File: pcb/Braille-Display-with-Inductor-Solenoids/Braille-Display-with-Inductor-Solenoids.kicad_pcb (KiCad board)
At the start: 2 copper layers, 58.2 x 57.4 mm, 60 parts, among them J1 Screw_Terminal_01x02, J2 Screw_Terminal_01x02, J3 Screw_Terminal_01x02, SW1 SW_Push, SW2 SW_Push, U1 RP2040-Zero, U2 TPIC6595, U3 TPIC6595, U4 TPIC6595

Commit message: Remove symbol and footprint libraries
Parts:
- L1, L10, L11, L12, L13, L14, L15, L16, L17, L18, L2, L3, L4, L5, L6, L7, L8, L9: footprint 00-project-footprint-lib:Inductor_0805_2012Metric_SMD_Vertical_Square -> 00-project-footprints:Inductor_0805_2012Metric_SMD_Vertical_Square
- SW1, SW2: footprint 00-project-footprint-lib:PushButtonSMD_2.93x3.9 -> 00-project-footprints:PushButtonSMD_2.93x3.9
- U1: footprint 00-project-footprint-lib:RP2040 Zero -> 00-project-footprints:RP2040 Zero

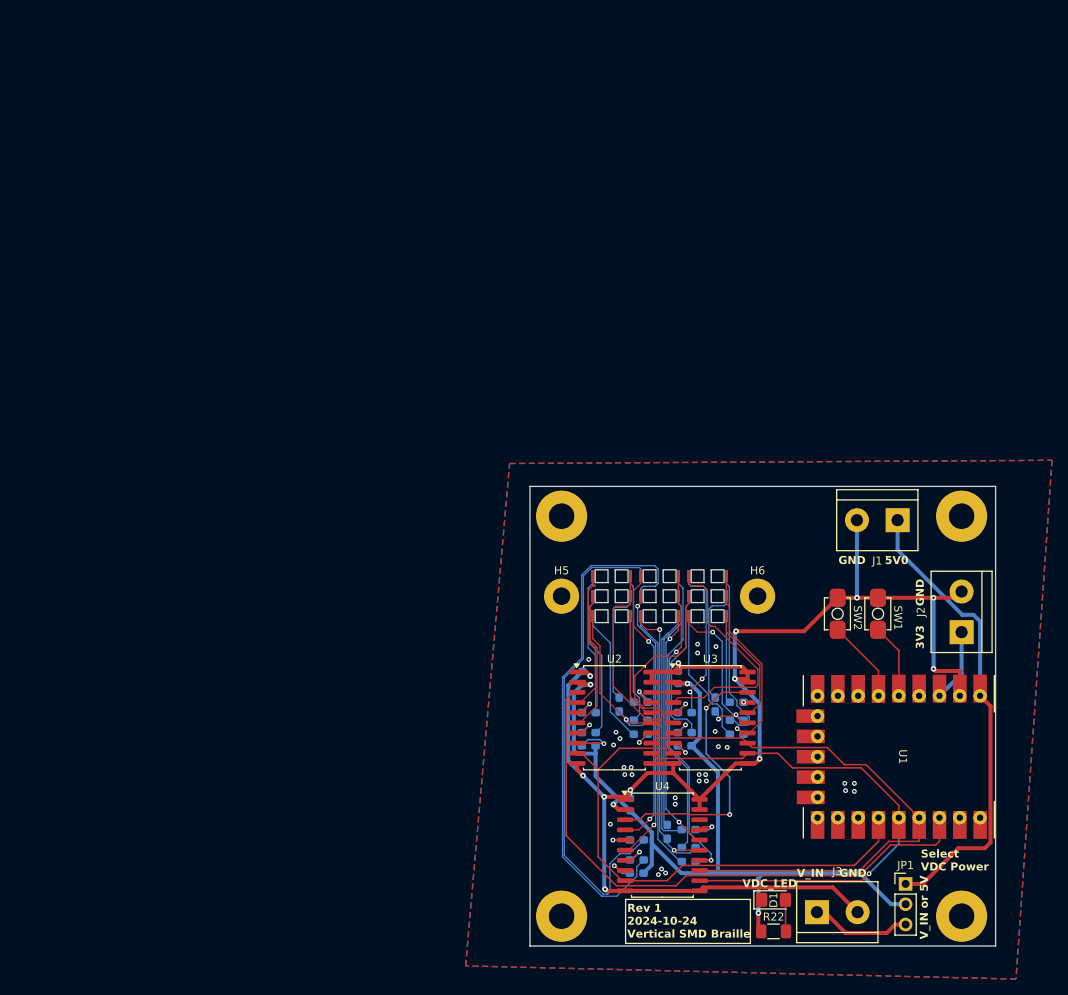
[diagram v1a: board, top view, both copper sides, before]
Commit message: Add both inductors on same PCB, switch to new drivers
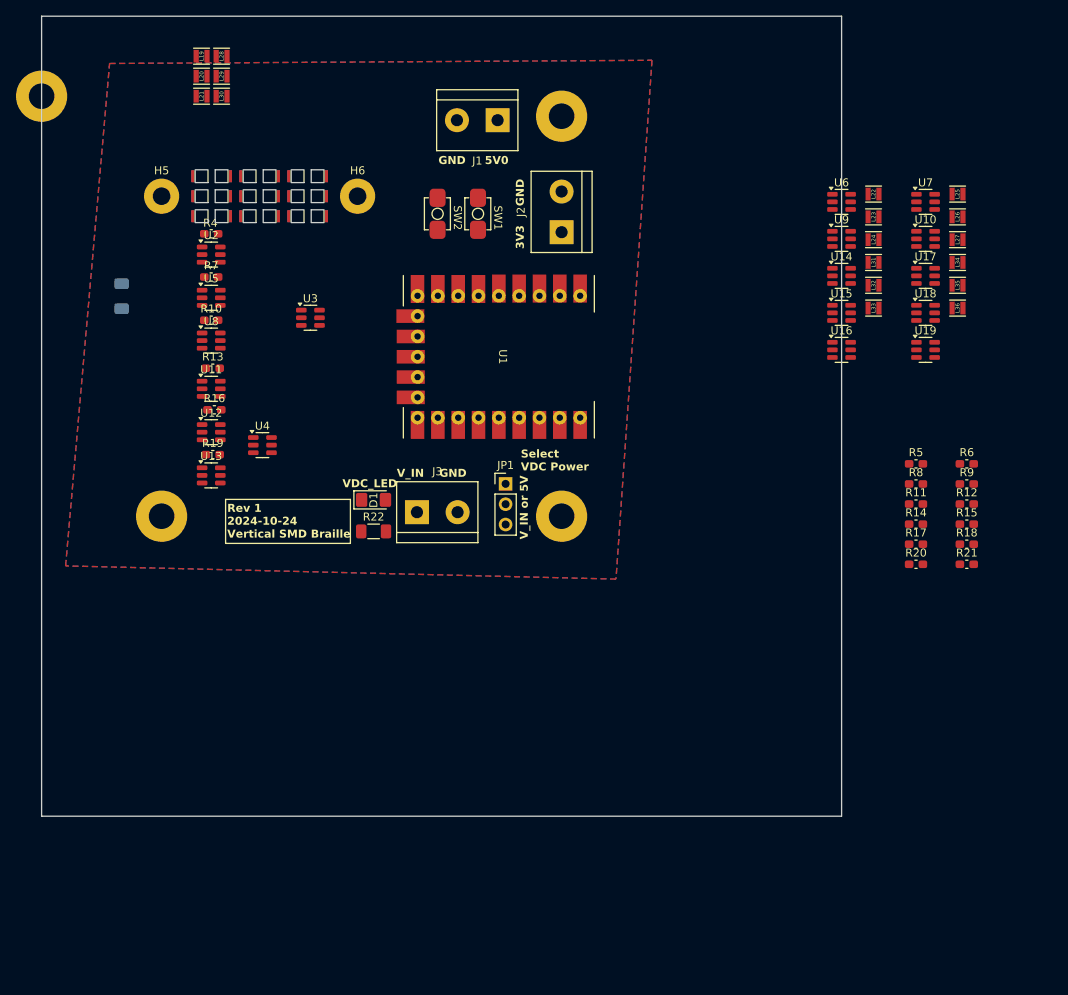
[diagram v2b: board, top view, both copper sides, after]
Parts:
- removed C2, C3: 100n, Capacitor_SMD:C_0603_1608Metric
- removed R1, R2, R3: 10k, Capacitor_SMD:C_0603_1608Metric_Pad1.08x0.95mm_HandSolder
- added L19: L, 00-project-footprints:Inductor_VLS201612CX, F.Cu at (50.0, 35.0)
- added L20: L, 00-project-footprints:Inductor_VLS201612CX, F.Cu at (50.0, 37.5)
- added L21: L, 00-project-footprints:Inductor_VLS201612CX, F.Cu at (50.0, 40.0)
- added L22: L, 00-project-footprints:Inductor_VLS201612CX, F.Cu at (134.0, 52.2)
- added L23: L, 00-project-footprints:Inductor_VLS201612CX, F.Cu at (134.0, 55.1)
- added L24: L, 00-project-footprints:Inductor_VLS201612CX, F.Cu at (134.0, 57.9)
- added L25: L, 00-project-footprints:Inductor_VLS201612CX, F.Cu at (144.5, 52.2)
- added L26: L, 00-project-footprints:Inductor_VLS201612CX, F.Cu at (144.5, 55.1)
- added L27: L, 00-project-footprints:Inductor_VLS201612CX, F.Cu at (144.5, 57.9)
- added L28: L, 00-project-footprints:Inductor_VLS201612CX, F.Cu at (52.5, 35.0)
- added L29: L, 00-project-footprints:Inductor_VLS201612CX, F.Cu at (52.5, 37.5)
- added L30: L, 00-project-footprints:Inductor_VLS201612CX, F.Cu at (52.5, 40.0)
- added L31: L, 00-project-footprints:Inductor_VLS201612CX, F.Cu at (134.0, 60.8)
- added L32: L, 00-project-footprints:Inductor_VLS201612CX, F.Cu at (134.0, 63.6)
- added L33: L, 00-project-footprints:Inductor_VLS201612CX, F.Cu at (134.0, 66.5)
- added L34: L, 00-project-footprints:Inductor_VLS201612CX, F.Cu at (144.5, 60.8)
- added L35: L, 00-project-footprints:Inductor_VLS201612CX, F.Cu at (144.5, 63.6)
- added L36: L, 00-project-footprints:Inductor_VLS201612CX, F.Cu at (144.5, 66.5)
- added U10: AD116, Package_TO_SOT_SMD:SOT-23-6, F.Cu at (140.5, 57.8)
- added U11: AD116, Package_TO_SOT_SMD:SOT-23-6, F.Cu at (51.2, 76.6)
- added U12: AD116, Package_TO_SOT_SMD:SOT-23-6, F.Cu at (51.2, 82.0)
- added U13: AD116, Package_TO_SOT_SMD:SOT-23-6, F.Cu at (51.2, 87.4)
- added U14: AD116, Package_TO_SOT_SMD:SOT-23-6, F.Cu at (130.0, 62.5)
- added U15: AD116, Package_TO_SOT_SMD:SOT-23-6, F.Cu at (130.0, 67.1)
- added U16: AD116, Package_TO_SOT_SMD:SOT-23-6, F.Cu at (130.0, 71.7)
- added U17: AD116, Package_TO_SOT_SMD:SOT-23-6, F.Cu at (140.5, 62.5)
- added U18: AD116, Package_TO_SOT_SMD:SOT-23-6, F.Cu at (140.5, 67.1)
- added U19: AD116, Package_TO_SOT_SMD:SOT-23-6, F.Cu at (140.5, 71.7)
- added U5: AD116, Package_TO_SOT_SMD:SOT-23-6, F.Cu at (51.2, 65.2)
- added U6: AD116, Package_TO_SOT_SMD:SOT-23-6, F.Cu at (130.0, 53.2)
- added U7: AD116, Package_TO_SOT_SMD:SOT-23-6, F.Cu at (140.5, 53.2)
- added U8: AD116, Package_TO_SOT_SMD:SOT-23-6, F.Cu at (51.2, 70.5)
- added U9: AD116, Package_TO_SOT_SMD:SOT-23-6, F.Cu at (130.0, 57.8)
- C1: value 100n -> 10u; footprint Capacitor_SMD:C_0603_1608Metric -> Capacitor_SMD:C_1206_3216Metric_Pad1.33x1.80mm_HandSolder
- R10, R11, R12, R13, R14, R15, R16, R17, R18, R19, R20, R21, R4, R5, R6, R7, R8, R9: moved to F.Cu
- U2, U3, U4: value TPIC6595 -> AD116; footprint Package_SO:SOIC-20W_7.5x12.8mm_P1.27mm -> Package_TO_SOT_SMD:SOT-23-6
- moved H1 83.6 mm to (30.0, 40.0)
- moved U2 76.8 mm to (51.2, 59.8)
- moved R4 76.2 mm to (51.2, 57.2), turned to 180 degrees
- moved C1 74.8 mm to (40.0, 65.0)
- moved R10 74.6 mm to (51.2, 68.0), turned to 0 degrees
- moved R7 74.0 mm to (51.2, 62.6)
- moved D1 70.7 mm to (71.5, 90.5)
- moved JP1 70.7 mm to (88.0, 88.5)
- moved SW1 70.7 mm to (84.5, 54.7)
- moved H2 70.7 mm to (95.0, 42.5)
- moved H3 70.7 mm to (45.0, 92.5)
- moved H4 70.7 mm to (95.0, 92.5)
- moved H5 70.7 mm to (45.0, 52.5)
- moved H6 70.7 mm to (69.5, 52.5)
- moved J1 70.7 mm to (87.0, 43.0)
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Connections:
- C1 pad 1: VDC -> +3V3
- L10 pad 1: /Braille_Cell1/DOT3_B -> /Braille_Cell1/DOT4_A
- L11 pad 1: /Braille_Cell1/DOT3_B -> /Braille_Cell1/DOT5_A
- L16 pad 1: /Braille_Cell2/DOT3_B -> /Braille_Cell2/DOT4_A
- L17 pad 1: /Braille_Cell2/DOT3_B -> /Braille_Cell2/DOT5_A
- L4 pad 1: /Braille_Cell/DOT3_B -> /Braille_Cell/DOT4_A
- L5 pad 1: /Braille_Cell/DOT3_B -> /Braille_Cell/DOT5_A
- R13 pad 2: /Braille_Cell/DOT3_A -> /Braille_Cell/DOT4_B
- R14 pad 2: /Braille_Cell1/DOT3_A -> /Braille_Cell1/DOT4_B
- R15 pad 2: /Braille_Cell2/DOT3_A -> /Braille_Cell2/DOT4_B
- R16 pad 2: /Braille_Cell/DOT3_A -> /Braille_Cell/DOT5_B
- R17 pad 2: /Braille_Cell1/DOT3_A -> /Braille_Cell1/DOT5_B
- R18 pad 2: /Braille_Cell2/DOT3_A -> /Braille_Cell2/DOT5_B
- U2 pad 1: GND -> /Braille_Cell/DOT1_B
- U2 pad 2: VDC -> GND
- U2 pad 3: /SHIFT_SER_IN -> /Braille_Cell/DOT1_B_CTRL
- U2 pad 4: /Braille_Cell/DOT1_A -> /Braille_Cell/DOT1_A_CTRL
- U2 pad 5: /Braille_Cell/DOT1_B -> VDC
- U2 pad 6: /Braille_Cell/DOT2_A -> /Braille_Cell/DOT1_A
- U3 pad 1: GND -> /Braille_Cell1/DOT1_B
- U3 pad 2: VDC -> GND
- U3 pad 3: /Braille_Cell/SER_OUT -> /Braille_Cell1/DOT1_B_CTRL
- U3 pad 4: /Braille_Cell1/DOT1_A -> /Braille_Cell1/DOT1_A_CTRL
- U3 pad 5: /Braille_Cell1/DOT1_B -> VDC
- U3 pad 6: /Braille_Cell1/DOT2_A -> /Braille_Cell1/DOT1_A
- U4 pad 1: GND -> /Braille_Cell2/DOT1_B
- U4 pad 2: VDC -> GND
- U4 pad 3: /Braille_Cell1/SER_OUT -> /Braille_Cell2/DOT1_B_CTRL
- U4 pad 4: /Braille_Cell2/DOT1_A -> /Braille_Cell2/DOT1_A_CTRL
- U4 pad 5: /Braille_Cell2/DOT1_B -> VDC
- U4 pad 6: /Braille_Cell2/DOT2_A -> /Braille_Cell2/DOT1_A
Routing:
- net GND: track 189.5 -> 0.00 mm, vias 40 -> 0
- net VDC: track 109.0 -> 0.00 mm, vias 4 -> 0
- net /SHIFT_SER_IN: track 73.3 -> 0.00 mm
- net /SHIFT_SRCK: track 69.7 -> 0.00 mm
- net /SHIFT_RCLK: track 66.7 -> 0.00 mm, vias 1 -> 0
- net /SHIFT_G: track 66.4 -> 0.00 mm
- net Net-(L14-Pad2): track 66.3 -> 0.00 mm
- net Net-(L13-Pad2): track 61.3 -> 0.00 mm
- net +5V: track 59.6 -> 0.00 mm
- net /Braille_Cell2/DOT3_B: track 42.0 -> 0.00 mm, vias 2 -> 0
- net /Braille_Cell2/DOT3_A: track 38.2 -> 0.00 mm, vias 2 -> 0
- net Net-(L16-Pad2): track 36.3 -> 0.00 mm
- net /Braille_Cell2/DOT1_A: track 35.6 -> 0.00 mm, vias 2 -> 0
- net /Braille_Cell2/DOT2_A: track 34.7 -> 0.00 mm, vias 2 -> 0
- net /Braille_Cell1/SER_OUT: track 33.9 -> 0.00 mm, vias 2 -> 0
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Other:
- board size 58.2 x 57.4 mm -> 100 x 100 mm

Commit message: Do layout
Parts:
- moved R6 87.3 mm to (63.2, 57.2), turned to 180 degrees
- moved R5 87.0 mm to (57.2, 57.2), turned to 180 degrees
- moved R9 86.4 mm to (63.2, 62.6)
- moved R8 86.1 mm to (57.2, 62.6)
- moved R12 85.6 mm to (63.2, 68.0)
- moved R11 85.3 mm to (57.2, 68.0)
- moved R15 84.5 mm to (63.4, 74.0)
- moved L27 84.4 mm to (62.0, 40.0)
- moved L26 84.3 mm to (62.0, 37.5)
- moved L25 84.3 mm to (62.0, 35.0)
- moved L36 84.3 mm to (64.5, 40.0)
- moved R14 84.2 mm to (57.4, 74.0)
- moved L35 84.2 mm to (64.5, 37.5)
- moved L34 84.0 mm to (64.5, 35.0)
- moved R18 83.8 mm to (63.6, 79.2)
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
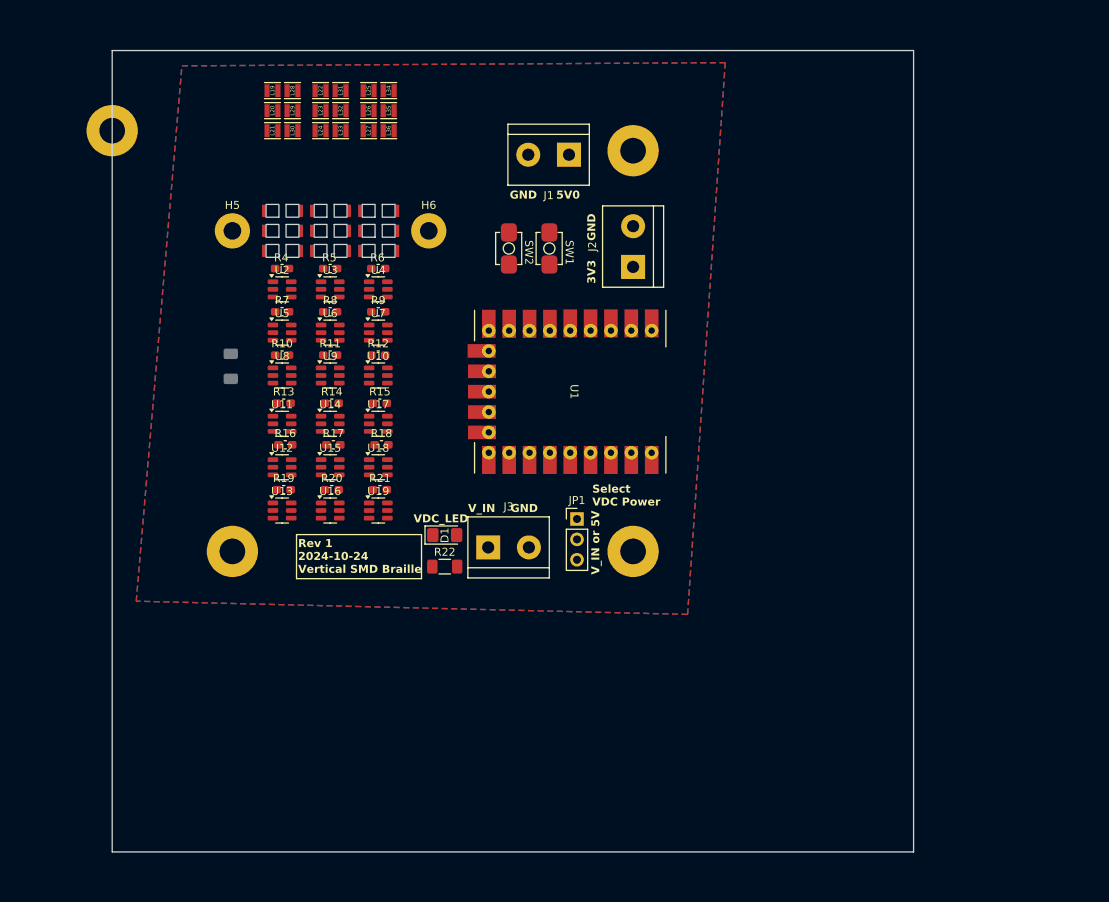
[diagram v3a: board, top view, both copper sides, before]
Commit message: Add breakouts, shrink SMD vertical inductor cutouts, add braille cell (4x now)
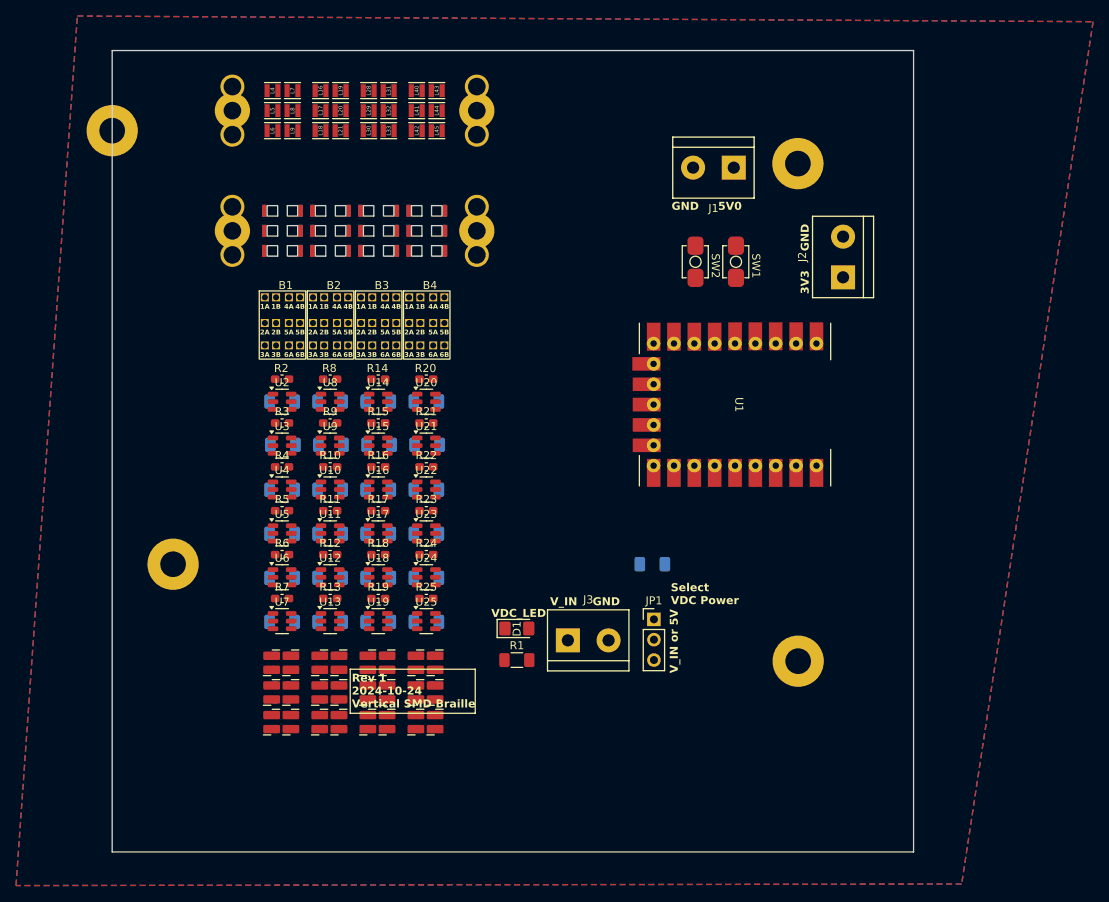
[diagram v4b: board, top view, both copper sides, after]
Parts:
- added B1: ~, 00-project-footprints:Braille_Cell_Breakout, F.Cu at (51.2, 64.0)
- added B2: ~, 00-project-footprints:Braille_Cell_Breakout, F.Cu at (57.2, 64.0)
- added B3: ~, 00-project-footprints:Braille_Cell_Breakout, F.Cu at (63.2, 64.0)
- added B4: ~, 00-project-footprints:Braille_Cell_Breakout, F.Cu at (69.2, 64.0)
- added C10: 10u, Capacitor_SMD:C_1206_3216Metric_Pad1.33x1.80mm_HandSolder, B.Cu at (51.2, 84.8)
- added C11: 10u, Capacitor_SMD:C_1206_3216Metric_Pad1.33x1.80mm_HandSolder, B.Cu at (57.2, 84.8)
- added C12: 10u, Capacitor_SMD:C_1206_3216Metric_Pad1.33x1.80mm_HandSolder, B.Cu at (63.2, 84.8)
- added C13: 10u, Capacitor_SMD:C_1206_3216Metric_Pad1.33x1.80mm_HandSolder, B.Cu at (69.2, 84.8)
- added C14: 10u, Capacitor_SMD:C_1206_3216Metric_Pad1.33x1.80mm_HandSolder, B.Cu at (51.2, 90.3)
- added C15: 10u, Capacitor_SMD:C_1206_3216Metric_Pad1.33x1.80mm_HandSolder, B.Cu at (57.2, 90.3)
- added C16: 10u, Capacitor_SMD:C_1206_3216Metric_Pad1.33x1.80mm_HandSolder, B.Cu at (63.2, 90.3)
- added C17: 10u, Capacitor_SMD:C_1206_3216Metric_Pad1.33x1.80mm_HandSolder, B.Cu at (69.2, 90.3)
- added C18: 10u, Capacitor_SMD:C_1206_3216Metric_Pad1.33x1.80mm_HandSolder, B.Cu at (51.2, 95.8)
- added C19: 10u, Capacitor_SMD:C_1206_3216Metric_Pad1.33x1.80mm_HandSolder, B.Cu at (57.2, 95.8)
- added C2: 10u, Capacitor_SMD:C_1206_3216Metric_Pad1.33x1.80mm_HandSolder, B.Cu at (51.2, 73.8)
- added C20: 10u, Capacitor_SMD:C_1206_3216Metric_Pad1.33x1.80mm_HandSolder, B.Cu at (63.2, 95.8)
- added C21: 10u, Capacitor_SMD:C_1206_3216Metric_Pad1.33x1.80mm_HandSolder, B.Cu at (69.2, 95.8)
- added C22: 10u, Capacitor_SMD:C_1206_3216Metric_Pad1.33x1.80mm_HandSolder, B.Cu at (51.2, 101.3)
- added C23: 10u, Capacitor_SMD:C_1206_3216Metric_Pad1.33x1.80mm_HandSolder, B.Cu at (57.2, 101.3)
- added C24: 10u, Capacitor_SMD:C_1206_3216Metric_Pad1.33x1.80mm_HandSolder, B.Cu at (63.2, 101.3)
- added C25: 10u, Capacitor_SMD:C_1206_3216Metric_Pad1.33x1.80mm_HandSolder, B.Cu at (69.2, 101.3)
- added C3: 10u, Capacitor_SMD:C_1206_3216Metric_Pad1.33x1.80mm_HandSolder, B.Cu at (57.2, 73.8)
- added C4: 10u, Capacitor_SMD:C_1206_3216Metric_Pad1.33x1.80mm_HandSolder, B.Cu at (63.2, 73.8)
- added C5: 10u, Capacitor_SMD:C_1206_3216Metric_Pad1.33x1.80mm_HandSolder, B.Cu at (69.2, 73.8)
- added C6: 10u, Capacitor_SMD:C_1206_3216Metric_Pad1.33x1.80mm_HandSolder, B.Cu at (51.3, 79.2)
- added C7: 10u, Capacitor_SMD:C_1206_3216Metric_Pad1.33x1.80mm_HandSolder, B.Cu at (57.3, 79.2)
- added C8: 10u, Capacitor_SMD:C_1206_3216Metric_Pad1.33x1.80mm_HandSolder, B.Cu at (63.3, 79.2)
- added C9: 10u, Capacitor_SMD:C_1206_3216Metric_Pad1.33x1.80mm_HandSolder, B.Cu at (69.3, 79.2)
- added D10: LED_Dual_Bidirectional, 00-project-footprints:LED_0603_1608Metric_HandSolder_2x_Reverse, F.Cu at (49.9, 110.1)
- added D11: LED_Dual_Bidirectional, 00-project-footprints:LED_0603_1608Metric_HandSolder_2x_Reverse, F.Cu at (52.3, 110.1)
- added D12: LED_Dual_Bidirectional, 00-project-footprints:LED_0603_1608Metric_HandSolder_2x_Reverse, F.Cu at (55.9, 110.1)
- added D13: LED_Dual_Bidirectional, 00-project-footprints:LED_0603_1608Metric_HandSolder_2x_Reverse, F.Cu at (58.3, 110.1)
- added D14: LED_Dual_Bidirectional, 00-project-footprints:LED_0603_1608Metric_HandSolder_2x_Reverse, F.Cu at (61.9, 110.1)
- added D15: LED_Dual_Bidirectional, 00-project-footprints:LED_0603_1608Metric_HandSolder_2x_Reverse, F.Cu at (64.3, 110.1)
- added D16: LED_Dual_Bidirectional, 00-project-footprints:LED_0603_1608Metric_HandSolder_2x_Reverse, F.Cu at (67.9, 110.1)
- added D17: LED_Dual_Bidirectional, 00-project-footprints:LED_0603_1608Metric_HandSolder_2x_Reverse, F.Cu at (70.3, 110.1)
- added D18: LED_Dual_Bidirectional, 00-project-footprints:LED_0603_1608Metric_HandSolder_2x_Reverse, F.Cu at (49.9, 113.8)
- added D19: LED_Dual_Bidirectional, 00-project-footprints:LED_0603_1608Metric_HandSolder_2x_Reverse, F.Cu at (52.3, 113.8)
- added D2: LED_Dual_Bidirectional, 00-project-footprints:LED_0603_1608Metric_HandSolder_2x_Reverse, F.Cu at (49.9, 106.4)
- added D20: LED_Dual_Bidirectional, 00-project-footprints:LED_0603_1608Metric_HandSolder_2x_Reverse, F.Cu at (55.9, 113.8)
- added D21: LED_Dual_Bidirectional, 00-project-footprints:LED_0603_1608Metric_HandSolder_2x_Reverse, F.Cu at (58.3, 113.8)
- added D22: LED_Dual_Bidirectional, 00-project-footprints:LED_0603_1608Metric_HandSolder_2x_Reverse, F.Cu at (61.9, 113.8)
- added D23: LED_Dual_Bidirectional, 00-project-footprints:LED_0603_1608Metric_HandSolder_2x_Reverse, F.Cu at (64.3, 113.8)
- added D24: LED_Dual_Bidirectional, 00-project-footprints:LED_0603_1608Metric_HandSolder_2x_Reverse, F.Cu at (67.9, 113.8)
- added D25: LED_Dual_Bidirectional, 00-project-footprints:LED_0603_1608Metric_HandSolder_2x_Reverse, F.Cu at (70.3, 113.8)
- added D3: LED_Dual_Bidirectional, 00-project-footprints:LED_0603_1608Metric_HandSolder_2x_Reverse, F.Cu at (55.9, 106.4)
- added D4: LED_Dual_Bidirectional, 00-project-footprints:LED_0603_1608Metric_HandSolder_2x_Reverse, F.Cu at (61.9, 106.4)
- added D5: LED_Dual_Bidirectional, 00-project-footprints:LED_0603_1608Metric_HandSolder_2x_Reverse, F.Cu at (67.9, 106.4)
- added D6: LED_Dual_Bidirectional, 00-project-footprints:LED_0603_1608Metric_HandSolder_2x_Reverse, F.Cu at (52.3, 106.4)
- added D7: LED_Dual_Bidirectional, 00-project-footprints:LED_0603_1608Metric_HandSolder_2x_Reverse, F.Cu at (58.3, 106.4)
- added D8: LED_Dual_Bidirectional, 00-project-footprints:LED_0603_1608Metric_HandSolder_2x_Reverse, F.Cu at (64.3, 106.4)
- added D9: LED_Dual_Bidirectional, 00-project-footprints:LED_0603_1608Metric_HandSolder_2x_Reverse, F.Cu at (70.3, 106.4)
- added H7: MountingHole_Pad, 00-project-footprints:Braille_Block_MountingHoles_M2_3x, F.Cu at (45.0, 37.5)
- added H8: MountingHole_Pad, 00-project-footprints:Braille_Block_MountingHoles_M2_3x, F.Cu at (75.5, 37.5)
- added L37: L, 00-project-footprints:Inductor_0805_2012Metric_SMD_Vertical_Square_Rev2_1.3mm, F.Cu at (68.0, 50.0)
- added L38: L, 00-project-footprints:Inductor_0805_2012Metric_SMD_Vertical_Square_Rev2_1.3mm, F.Cu at (68.0, 52.5)
- added L39: L, 00-project-footprints:Inductor_0805_2012Metric_SMD_Vertical_Square_Rev2_1.3mm, F.Cu at (68.0, 55.0)
- added L40: L, 00-project-footprints:Inductor_VLS201612CX, F.Cu at (68.0, 35.0)
- added L41: L, 00-project-footprints:Inductor_VLS201612CX, F.Cu at (68.0, 37.5)
- added L42: L, 00-project-footprints:Inductor_VLS201612CX, F.Cu at (68.0, 40.0)
- added L43: L, 00-project-footprints:Inductor_VLS201612CX, F.Cu at (70.5, 35.0)
- added L44: L, 00-project-footprints:Inductor_VLS201612CX, F.Cu at (70.5, 37.5)
- added L45: L, 00-project-footprints:Inductor_VLS201612CX, F.Cu at (70.5, 40.0)
- added L46: L, 00-project-footprints:Inductor_0805_2012Metric_SMD_Vertical_Square_Rev2_1.3mm, F.Cu at (70.5, 50.0)
- added L47: L, 00-project-footprints:Inductor_0805_2012Metric_SMD_Vertical_Square_Rev2_1.3mm, F.Cu at (70.5, 52.5)
- added L48: L, 00-project-footprints:Inductor_0805_2012Metric_SMD_Vertical_Square_Rev2_1.3mm, F.Cu at (70.5, 55.0)
- added R10: 20, Capacitor_SMD:C_0603_1608Metric_Pad1.08x0.95mm_HandSolder, F.Cu at (57.2, 82.0)
- added R23: 20, Capacitor_SMD:C_0603_1608Metric_Pad1.08x0.95mm_HandSolder, F.Cu at (69.2, 87.4)
- added R24: 20, Capacitor_SMD:C_0603_1608Metric_Pad1.08x0.95mm_HandSolder, F.Cu at (69.2, 92.9)
- added R25: 20, Capacitor_SMD:C_0603_1608Metric_Pad1.08x0.95mm_HandSolder, F.Cu at (69.2, 98.4)
- added R26: 5k1, Resistor_SMD:R_0603_1608Metric, B.Cu at (51.2, 105.5)
- added R27: 5k1, Resistor_SMD:R_0603_1608Metric, B.Cu at (57.2, 105.5)
- added R28: 5k1, Resistor_SMD:R_0603_1608Metric, B.Cu at (63.2, 105.5)
- added R29: 5k1, Resistor_SMD:R_0603_1608Metric, B.Cu at (69.2, 105.5)
- added R30: 5k1, Resistor_SMD:R_0603_1608Metric, B.Cu at (51.1, 109.2)
- added R31: 5k1, Resistor_SMD:R_0603_1608Metric, B.Cu at (57.1, 109.2)
- added R32: 5k1, Resistor_SMD:R_0603_1608Metric, B.Cu at (63.1, 109.2)
- added R33: 5k1, Resistor_SMD:R_0603_1608Metric, B.Cu at (69.1, 109.2)
- added R34: 5k1, Resistor_SMD:R_0603_1608Metric, B.Cu at (51.1, 112.9)
- added R35: 5k1, Resistor_SMD:R_0603_1608Metric, B.Cu at (57.1, 112.9)
- added R36: 5k1, Resistor_SMD:R_0603_1608Metric, B.Cu at (63.1, 112.9)
- added R37: 5k1, Resistor_SMD:R_0603_1608Metric, B.Cu at (69.1, 112.9)
- added R38: 5k1, Resistor_SMD:R_0603_1608Metric, B.Cu at (51.2, 107.3)
- added R39: 5k1, Resistor_SMD:R_0603_1608Metric, B.Cu at (57.2, 107.3)
- added R40: 5k1, Resistor_SMD:R_0603_1608Metric, B.Cu at (63.2, 107.3)
- added R41: 5k1, Resistor_SMD:R_0603_1608Metric, B.Cu at (69.2, 107.3)
- added R42: 5k1, Resistor_SMD:R_0603_1608Metric, B.Cu at (51.1, 111.0)
- added R43: 5k1, Resistor_SMD:R_0603_1608Metric, B.Cu at (57.1, 111.0)
- added R44: 5k1, Resistor_SMD:R_0603_1608Metric, B.Cu at (63.1, 111.0)
- added R45: 5k1, Resistor_SMD:R_0603_1608Metric, B.Cu at (69.1, 111.0)
- added R46: 5k1, Resistor_SMD:R_0603_1608Metric, B.Cu at (51.1, 114.7)
- added R47: 5k1, Resistor_SMD:R_0603_1608Metric, B.Cu at (57.1, 114.7)
- added R48: 5k1, Resistor_SMD:R_0603_1608Metric, B.Cu at (63.1, 114.7)
- added R49: 5k1, Resistor_SMD:R_0603_1608Metric, B.Cu at (69.1, 114.7)
- added R8: 20, Capacitor_SMD:C_0603_1608Metric_Pad1.08x0.95mm_HandSolder, F.Cu at (57.2, 71.0)
- added R9: 20, Capacitor_SMD:C_0603_1608Metric_Pad1.08x0.95mm_HandSolder, F.Cu at (57.2, 76.5)
- added U20: AD116, Package_TO_SOT_SMD:SOT-23-6, F.Cu at (69.2, 73.8)
- added U21: AD116, Package_TO_SOT_SMD:SOT-23-6, F.Cu at (69.2, 79.3)
- added U22: AD116, Package_TO_SOT_SMD:SOT-23-6, F.Cu at (69.2, 84.8)
- added U23: AD116, Package_TO_SOT_SMD:SOT-23-6, F.Cu at (69.2, 90.2)
- added U24: AD116, Package_TO_SOT_SMD:SOT-23-6, F.Cu at (69.2, 95.7)
- added U25: AD116, Package_TO_SOT_SMD:SOT-23-6, F.Cu at (69.2, 101.2)
- H5, H6: footprint MountingHole:MountingHole_2.2mm_M2_Pad -> 00-project-footprints:Braille_Block_MountingHoles_M2_3x
- L1, L2, L3: footprint 00-project-footprints:Inductor_0805_2012Metric_SMD_Vertical_Square -> 00-project-footprints:Inductor_0805_2012Metric_SMD_Vertical_Square_Rev2_1.3mm
- L10: renamed from L4; footprint 00-project-footprints:Inductor_0805_2012Metric_SMD_Vertical_Square -> 00-project-footprints:Inductor_0805_2012Metric_SMD_Vertical_Square_Rev2_1.3mm
- L11: renamed from L5; footprint 00-project-footprints:Inductor_0805_2012Metric_SMD_Vertical_Square -> 00-project-footprints:Inductor_0805_2012Metric_SMD_Vertical_Square_Rev2_1.3mm
- L12: renamed from L6; footprint 00-project-footprints:Inductor_0805_2012Metric_SMD_Vertical_Square -> 00-project-footprints:Inductor_0805_2012Metric_SMD_Vertical_Square_Rev2_1.3mm
- L13: renamed from L7; footprint 00-project-footprints:Inductor_0805_2012Metric_SMD_Vertical_Square -> 00-project-footprints:Inductor_0805_2012Metric_SMD_Vertical_Square_Rev2_1.3mm
- L14: renamed from L8; footprint 00-project-footprints:Inductor_0805_2012Metric_SMD_Vertical_Square -> 00-project-footprints:Inductor_0805_2012Metric_SMD_Vertical_Square_Rev2_1.3mm
- L15: renamed from L9; footprint 00-project-footprints:Inductor_0805_2012Metric_SMD_Vertical_Square -> 00-project-footprints:Inductor_0805_2012Metric_SMD_Vertical_Square_Rev2_1.3mm
- L16: renamed from L10; footprint 00-project-footprints:Inductor_0805_2012Metric_SMD_Vertical_Square -> 00-project-footprints:Inductor_VLS201612CX
- L17: renamed from L11; footprint 00-project-footprints:Inductor_0805_2012Metric_SMD_Vertical_Square -> 00-project-footprints:Inductor_VLS201612CX
- L18: renamed from L12; footprint 00-project-footprints:Inductor_0805_2012Metric_SMD_Vertical_Square -> 00-project-footprints:Inductor_VLS201612CX
- L19: renamed from L13; footprint 00-project-footprints:Inductor_0805_2012Metric_SMD_Vertical_Square -> 00-project-footprints:Inductor_VLS201612CX
- L20: renamed from L14; footprint 00-project-footprints:Inductor_0805_2012Metric_SMD_Vertical_Square -> 00-project-footprints:Inductor_VLS201612CX
- L21: renamed from L15; footprint 00-project-footprints:Inductor_0805_2012Metric_SMD_Vertical_Square -> 00-project-footprints:Inductor_VLS201612CX
- L22: renamed from L16; footprint 00-project-footprints:Inductor_0805_2012Metric_SMD_Vertical_Square -> 00-project-footprints:Inductor_0805_2012Metric_SMD_Vertical_Square_Rev2_1.3mm
- L23: renamed from L17; footprint 00-project-footprints:Inductor_0805_2012Metric_SMD_Vertical_Square -> 00-project-footprints:Inductor_0805_2012Metric_SMD_Vertical_Square_Rev2_1.3mm
- L24: renamed from L18; footprint 00-project-footprints:Inductor_0805_2012Metric_SMD_Vertical_Square -> 00-project-footprints:Inductor_0805_2012Metric_SMD_Vertical_Square_Rev2_1.3mm
- L25: renamed from L22; footprint 00-project-footprints:Inductor_VLS201612CX -> 00-project-footprints:Inductor_0805_2012Metric_SMD_Vertical_Square_Rev2_1.3mm
- L26: renamed from L23; footprint 00-project-footprints:Inductor_VLS201612CX -> 00-project-footprints:Inductor_0805_2012Metric_SMD_Vertical_Square_Rev2_1.3mm
- L27: renamed from L24; footprint 00-project-footprints:Inductor_VLS201612CX -> 00-project-footprints:Inductor_0805_2012Metric_SMD_Vertical_Square_Rev2_1.3mm
- L34, L35, L36: footprint 00-project-footprints:Inductor_VLS201612CX -> 00-project-footprints:Inductor_0805_2012Metric_SMD_Vertical_Square_Rev2_1.3mm
- moved C1 58.1 mm to (97.4, 94.1), turned to 180 degrees
- moved R12 36.2 mm to (57.2, 92.9), turned to 0 degrees
- moved R13 35.8 mm to (57.2, 98.4)
- moved U13 31.2 mm to (57.2, 101.2)
- moved R11 30.2 mm to (57.2, 87.4), turned to 0 degrees
- moved J2 26.2 mm to (121.2, 58.3)
- moved U11 25.8 mm to (57.2, 90.2)
- moved U12 25.2 mm to (57.2, 95.7)
- moved H4 24.7 mm to (115.6, 106.2)
- moved SW1 23.3 mm to (107.8, 56.4)
- moved SW2 23.3 mm to (102.8, 56.4)
- moved H2 20.6 mm to (115.6, 44.1)
- moved J1 20.6 mm to (107.6, 44.6)
- moved U1 20.6 mm to (94.9, 64.0)
- moved U9 20.4 mm to (57.2, 79.3)
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- renumbered L25 to L28, L26 to L29, L27 to L30, L19 to L4, L20 to L5, L21 to L6, L28 to L7, L29 to L8, L30 to L9, R22 to R1, R5 to R11, R6 to R12, R8 to R13, R9 to R14, R11 to R15, R12 to R16, R14 to R17, R15 to R18, R17 to R19, R4 to R2, R18 to R20, R20 to R21, R21 to R22, R7 to R3, R10 to R4, R13 to R5, R16 to R6, R19 to R7, U6 to U10, U7 to U11, U9 to U12, U10 to U13, U5 to U3, U8 to U4, U11 to U5, U12 to U6, U13 to U7, U3 to U8, U4 to U9
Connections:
- L13 pad 2: Net-(L22-Pad2) -> Net-(B2-1B)
- L14 pad 2: Net-(L23-Pad2) -> Net-(B2-2B)
- L15 pad 2: Net-(L24-Pad2) -> Net-(B2-3B)
- L16 pad 1: /Braille_Cell1/DOT4_A -> /Braille_Cell1/DOT1_A
- L16 pad 2: Net-(L10-Pad2) -> Net-(B2-1B)
- L17 pad 1: /Braille_Cell1/DOT5_A -> /Braille_Cell1/DOT2_A
- L17 pad 2: Net-(L11-Pad2) -> Net-(B2-2B)
- L18 pad 1: /Braille_Cell1/DOT6_A -> /Braille_Cell1/DOT3_A
- L18 pad 2: Net-(L12-Pad2) -> Net-(B2-3B)
- L19 pad 1: /Braille_Cell2/DOT1_A -> /Braille_Cell1/DOT4_A
- L19 pad 2: Net-(L13-Pad2) -> Net-(B2-4B)
- L20 pad 1: /Braille_Cell2/DOT2_A -> /Braille_Cell1/DOT5_A
- L20 pad 2: Net-(L14-Pad2) -> Net-(B2-5B)
- L21 pad 1: /Braille_Cell2/DOT3_A -> /Braille_Cell1/DOT6_A
- L21 pad 2: Net-(L15-Pad2) -> Net-(B2-6B)
- L22 pad 1: /Braille_Cell2/DOT4_A -> /Braille_Cell1/DOT4_A
- L22 pad 2: Net-(L16-Pad2) -> Net-(B2-4B)
- L23 pad 1: /Braille_Cell2/DOT5_A -> /Braille_Cell1/DOT5_A
- L23 pad 2: Net-(L17-Pad2) -> Net-(B2-5B)
- L24 pad 1: /Braille_Cell2/DOT6_A -> /Braille_Cell1/DOT6_A
- L24 pad 2: Net-(L18-Pad2) -> Net-(B2-6B)
- L25 pad 1: /Braille_Cell1/DOT1_A -> /Braille_Cell2/DOT1_A
- L25 pad 2: Net-(L22-Pad2) -> Net-(B3-1B)
- L26 pad 1: /Braille_Cell1/DOT2_A -> /Braille_Cell2/DOT2_A
- L26 pad 2: Net-(L23-Pad2) -> Net-(B3-2B)
- L27 pad 1: /Braille_Cell1/DOT3_A -> /Braille_Cell2/DOT3_A
- L27 pad 2: Net-(L24-Pad2) -> Net-(B3-3B)
- L28 pad 2: Net-(L13-Pad2) -> Net-(B3-1B)
- L29 pad 2: Net-(L14-Pad2) -> Net-(B3-2B)
- L30 pad 2: Net-(L15-Pad2) -> Net-(B3-3B)
- L31 pad 1: /Braille_Cell1/DOT4_A -> /Braille_Cell2/DOT4_A
- L31 pad 2: Net-(L10-Pad2) -> Net-(B3-4B)
- L32 pad 1: /Braille_Cell1/DOT5_A -> /Braille_Cell2/DOT5_A
- L32 pad 2: Net-(L11-Pad2) -> Net-(B3-5B)
- L33 pad 1: /Braille_Cell1/DOT6_A -> /Braille_Cell2/DOT6_A
- L33 pad 2: Net-(L12-Pad2) -> Net-(B3-6B)
- L34 pad 2: Net-(L16-Pad2) -> Net-(B3-4B)
- L35 pad 2: Net-(L17-Pad2) -> Net-(B3-5B)
- L36 pad 2: Net-(L18-Pad2) -> Net-(B3-6B)
- R11 pad 1: /Braille_Cell1/DOT1_B -> Net-(B2-4B)
- R11 pad 2: Net-(L22-Pad2) -> /Braille_Cell1/DOT4_B
- R12 pad 1: /Braille_Cell2/DOT1_B -> Net-(B2-5B)
- R12 pad 2: Net-(L13-Pad2) -> /Braille_Cell1/DOT5_B
- R13 pad 1: /Braille_Cell1/DOT2_B -> Net-(B2-6B)
- R13 pad 2: Net-(L23-Pad2) -> /Braille_Cell1/DOT6_B
- R14 pad 1: /Braille_Cell2/DOT2_B -> /Braille_Cell2/DOT1_B
- R14 pad 2: Net-(L14-Pad2) -> Net-(B3-1B)
- R15 pad 1: /Braille_Cell1/DOT3_B -> /Braille_Cell2/DOT2_B
- R15 pad 2: Net-(L24-Pad2) -> Net-(B3-2B)
- R16 pad 2: Net-(L15-Pad2) -> Net-(B3-3B)
- R17 pad 1: Net-(L10-Pad2) -> Net-(B3-4B)
- R17 pad 2: /Braille_Cell1/DOT4_B -> /Braille_Cell2/DOT4_B
- R18 pad 1: Net-(L16-Pad2) -> Net-(B3-5B)
- R18 pad 2: /Braille_Cell2/DOT4_B -> /Braille_Cell2/DOT5_B
- R19 pad 1: Net-(L11-Pad2) -> Net-(B3-6B)
- R19 pad 2: /Braille_Cell1/DOT5_B -> /Braille_Cell2/DOT6_B
- R20 pad 1: Net-(L17-Pad2) -> /Braille_Cell3/DOT1_B
- R20 pad 2: /Braille_Cell2/DOT5_B -> Net-(B4-1B)
- R21 pad 1: Net-(L12-Pad2) -> /Braille_Cell3/DOT2_B
- R21 pad 2: /Braille_Cell1/DOT6_B -> Net-(B4-2B)
- R22 pad 1: Net-(L18-Pad2) -> /Braille_Cell3/DOT3_B
- R22 pad 2: /Braille_Cell2/DOT6_B -> Net-(B4-3B)
- U10 pad 1: /Braille_Cell1/DOT2_B -> /Braille_Cell1/DOT3_B
- U10 pad 3: /Braille_Cell1/DOT2_B_CTRL -> /Braille_Cell1/DOT3_B_CTRL
- U10 pad 4: /Braille_Cell1/DOT2_A_CTRL -> /Braille_Cell1/DOT3_A_CTRL
- U10 pad 6: /Braille_Cell1/DOT2_A -> /Braille_Cell1/DOT3_A
- U11 pad 1: /Braille_Cell2/DOT2_B -> /Braille_Cell1/DOT4_B
- U11 pad 3: /Braille_Cell2/DOT2_B_CTRL -> /Braille_Cell1/DOT4_B_CTRL
- U11 pad 4: /Braille_Cell2/DOT2_A_CTRL -> /Braille_Cell1/DOT4_A_CTRL
- U11 pad 6: /Braille_Cell2/DOT2_A -> /Braille_Cell1/DOT4_A
- U12 pad 1: /Braille_Cell1/DOT3_B -> /Braille_Cell1/DOT5_B
- U12 pad 3: /Braille_Cell1/DOT3_B_CTRL -> /Braille_Cell1/DOT5_B_CTRL
- U12 pad 4: /Braille_Cell1/DOT3_A_CTRL -> /Braille_Cell1/DOT5_A_CTRL
- U12 pad 6: /Braille_Cell1/DOT3_A -> /Braille_Cell1/DOT5_A
- U13 pad 1: /Braille_Cell2/DOT3_B -> /Braille_Cell1/DOT6_B
- U13 pad 3: /Braille_Cell2/DOT3_B_CTRL -> /Braille_Cell1/DOT6_B_CTRL
- U13 pad 4: /Braille_Cell2/DOT3_A_CTRL -> /Braille_Cell1/DOT6_A_CTRL
- U13 pad 6: /Braille_Cell2/DOT3_A -> /Braille_Cell1/DOT6_A
- U14 pad 1: /Braille_Cell1/DOT4_B -> /Braille_Cell2/DOT1_B
- U14 pad 3: /Braille_Cell1/DOT4_B_CTRL -> /Braille_Cell2/DOT1_B_CTRL
- U14 pad 4: /Braille_Cell1/DOT4_A_CTRL -> /Braille_Cell2/DOT1_A_CTRL
- U14 pad 6: /Braille_Cell1/DOT4_A -> /Braille_Cell2/DOT1_A
- U15 pad 1: /Braille_Cell1/DOT5_B -> /Braille_Cell2/DOT2_B
- U15 pad 3: /Braille_Cell1/DOT5_B_CTRL -> /Braille_Cell2/DOT2_B_CTRL
- U15 pad 4: /Braille_Cell1/DOT5_A_CTRL -> /Braille_Cell2/DOT2_A_CTRL
- U15 pad 6: /Braille_Cell1/DOT5_A -> /Braille_Cell2/DOT2_A
- U16 pad 1: /Braille_Cell1/DOT6_B -> /Braille_Cell2/DOT3_B
- U16 pad 3: /Braille_Cell1/DOT6_B_CTRL -> /Braille_Cell2/DOT3_B_CTRL
- U16 pad 4: /Braille_Cell1/DOT6_A_CTRL -> /Braille_Cell2/DOT3_A_CTRL
- U16 pad 6: /Braille_Cell1/DOT6_A -> /Braille_Cell2/DOT3_A
- U9 pad 1: /Braille_Cell2/DOT1_B -> /Braille_Cell1/DOT2_B
- U9 pad 3: /Braille_Cell2/DOT1_B_CTRL -> /Braille_Cell1/DOT2_B_CTRL
- U9 pad 4: /Braille_Cell2/DOT1_A_CTRL -> /Braille_Cell1/DOT2_A_CTRL
- U9 pad 6: /Braille_Cell2/DOT1_A -> /Braille_Cell1/DOT2_A
